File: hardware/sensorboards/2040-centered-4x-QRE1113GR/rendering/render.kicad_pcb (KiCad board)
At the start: 2 copper layers, 204.8 x 52 mm, 44 parts, among them J1 Conn_01x10_Male, U1 QRE1113GR, U2 QRE1113GR, U3 QRE1113GR, U4 QRE1113GR

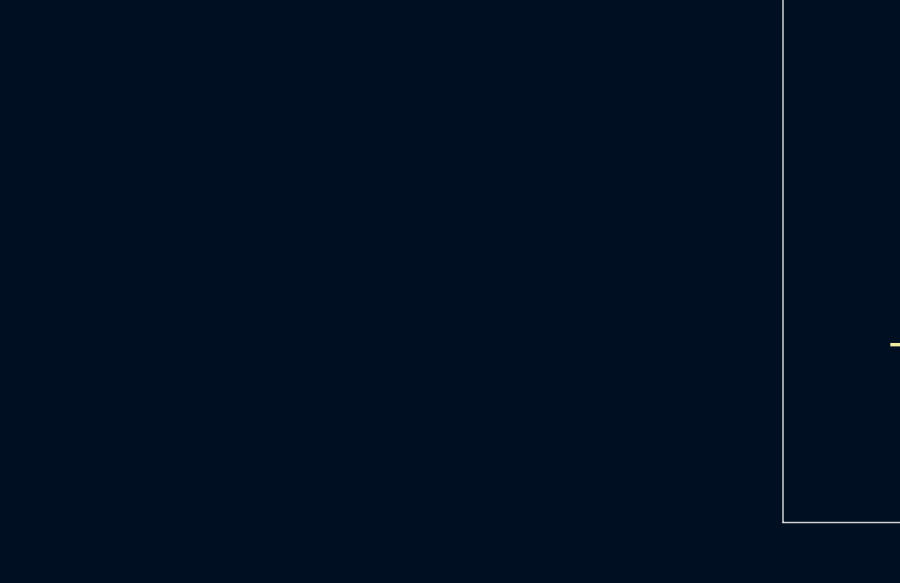
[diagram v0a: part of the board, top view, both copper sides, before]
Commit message: added another screen to show bottom, enlarged mock 3D model of QRE1113 which is not accurate
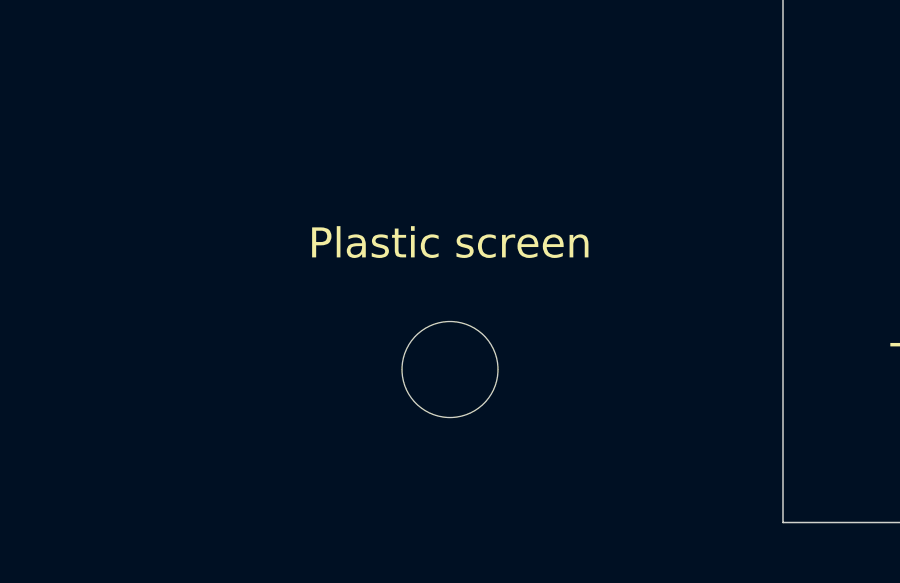
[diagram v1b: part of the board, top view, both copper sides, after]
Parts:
- added Plastic screen: MountingHole, Mounting_Holes:MountingHole_3.2mm_M3, F.Cu at (119.0, 107.2)
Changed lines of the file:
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@@
+    (model "${KICAD6_3DMODEL_DIR}/Package_TO_SOT_SMD.3dshapes/SOT-343_SC-70-4.step"
+      (offset (xyz 0 0 0))
+      (scale (xyz 2.1 1.3 3))
+      (rotate (xyz 0 0 0))
+    )
+  )
+  (footprint "OptoDevice:QRE1113GR" (layer "F.Cu")
+    (at 46.95 92.3)
+    (property "Sheetfile" "2040-centered-4x-QRE1113GR.kicad_sch")
+    (property "Sheetname" "")
+    (attr smd)
+    (fp_text reference "U2" (at 0 2.9 unlocked) (layer "F.SilkS")
+      (effects (font (size 1 1) (thickness 0.15)))
+    )
+    (fp_text value "QRE1113GR" (at 0 4.4 unlocked) (layer "F.Fab")
+      (effects (font (size 1 1) (thickness 0.15)))
+    )
+    (fp_text user "${REFERENCE}" (at 0 0 270 unlocked) (layer "F.Fab")
+      (effects (font (size 0.5 0.5) (thickness 0.075)))
+    )
+    (fp_line (start -1.45 -0.3) (end -1.45 0.3) (layer "F.SilkS") (width 0.24))
+    (fp_line (start -1.45 -1.8) (end 1.45 -1.8) (layer "F.SilkS") (width 0.24))
+    (fp_line (start 1.45 -0.3) (end 1.45 0.3) (layer "F.SilkS") (width 0.24))
+    (fp_line (start 1.45 1.4) (end 1.45 1.8) (layer "F.SilkS") (width 0.24))
+    (fp_line (start 1.45 -1.8) (end 1.45 -1.4) (layer "F.SilkS") (width 0.24))
+    (fp_line (start -0.825 1.8) (end -1.2 1.425) (layer "F.SilkS") (width 0.24))
+    (fp_line (start 1.45 1.8) (end -0.825 1.8) (layer "F.SilkS") (width 0.24))
+    (fp_line (start -1.45 -1.8) (end -1.45 -1.4) (layer "F.SilkS") (width 0.24))
+    (fp_rect (start -3.1 -2.1) (end 3.1 2.1) (layer "F.CrtYd") (width 0.05) (fill none))
+    (fp_line (start 1.45 1.8) (end -0.825 1.8) (layer "F.Fab") (width 0.1))
+    (fp_line (start 1.45 -1.8) (end 1.45 1.8) (layer "F.Fab") (width 0.1))
+    (fp_line (start -0.825 1.8) (end -1.45 1.175) (layer "F.Fab") (width 0.1))
+    (fp_line (start -1.45 1.175) (end -1.45 -1.8) (layer "F.Fab") (width 0.1))
+    (fp_line (start -1.45 -1.8) (end 1.45 -1.8) (layer "F.Fab") (width 0.1))
+    (pad "1" smd roundrect (at -2 0.9) (size 1.66 0.79) (layers "F.Cu" "F.Paste" "F.Mask") (roundrect_rratio 0.05)
+      (net 10 "Net-(TP1-Pad1)") (pinfunction "A") (pintype "passive"))
+    (pad "2" smd roundrect (at 2 0.9) (size 1.66 0.79) (layers "F.Cu" "F.Paste" "F.Mask") (roundrect_rratio 0.05)
+      (net 11 "Net-(TP2-Pad1)") (pinfunction "K") (pintype "passive"))
+    (pad "3" smd roundrect (at 2 -0.9) (size 1.66 0.79) (layers "F.Cu" "F.Paste" "F.Mask") (roundrect_rratio 0.05)
+      (net 13 "Net-(U2-Pad3)") (pintype "open_collector"))
+    (pad "4" smd roundrect (at -2 -0.9) (size 1.66 0.79) (layers "F.Cu" "F.Paste" "F.Mask") (roundrect_rratio 0.05)
+      (net 6 "/E2") (pintype "open_emitter"))
     (model "${KICAD6_3DMODEL_DIR}/Package_TO_SOT_SMD.3dshapes/SOT-343_SC-70-4.step"
       (offset (xyz 0 0 0))
@@
     )
   )
-  (footprint "OptoDevice:QRE1113GR" (layer "F.Cu")
-    (at 46.95 92.3)
-    (property "Sheetfile" "2040-centered-4x-QRE1113GR.kicad_sch")
-    (property "Sheetname" "")
-    (attr smd)
-    (fp_text reference "U2" (at 0 2.9 unlocked) (layer "F.SilkS")
-      (effects (font (size 1 1) (thickness 0.15)))
-    )
-    (fp_text value "QRE1113GR" (at 0 4.4 unlocked) (layer "F.Fab")
-      (effects (font (size 1 1) (thickness 0.15)))
-    )
-    (fp_text user "${REFERENCE}" (at 0 0 270 unlocked) (layer "F.Fab")
-      (effects (font (size 0.5 0.5) (thickness 0.075)))
-    )
-    (fp_line (start -1.45 -0.3) (end -1.45 0.3) (layer "F.SilkS") (width 0.24))
-    (fp_line (start -1.45 -1.8) (end 1.45 -1.8) (layer "F.SilkS") (width 0.24))
-    (fp_line (start 1.45 -0.3) (end 1.45 0.3) (layer "F.SilkS") (width 0.24))
-    (fp_line (start 1.45 1.4) (end 1.45 1.8) (layer "F.SilkS") (width 0.24))
-    (fp_line (start 1.45 -1.8) (end 1.45 -1.4) (layer "F.SilkS") (width 0.24))
-    (fp_line (start -0.825 1.8) (end -1.2 1.425) (layer "F.SilkS") (width 0.24))
-    (fp_line (start 1.45 1.8) (end -0.825 1.8) (layer "F.SilkS") (width 0.24))
-    (fp_line (start -1.45 -1.8) (end -1.45 -1.4) (layer "F.SilkS") (width 0.24))
-    (fp_rect (start -3.1 -2.1) (end 3.1 2.1) (layer "F.CrtYd") (width 0.05) (fill none))
-    (fp_line (start 1.45 1.8) (end -0.825 1.8) (layer "F.Fab") (width 0.1))
-    (fp_line (start 1.45 -1.8) (end 1.45 1.8) (layer "F.Fab") (width 0.1))
-    (fp_line (start -0.825 1.8) (end -1.45 1.175) (layer "F.Fab") (width 0.1))
-    (fp_line (start -1.45 1.175) (end -1.45 -1.8) (layer "F.Fab") (width 0.1))
-    (fp_line (start -1.45 -1.8) (end 1.45 -1.8) (layer "F.Fab") (width 0.1))
-    (pad "1" smd roundrect (at -2 0.9) (size 1.66 0.79) (layers "F.Cu" "F.Paste" "F.Mask") (roundrect_rratio 0.05)
-      (net 10 "Net-(TP1-Pad1)") (pinfunction "A") (pintype "passive"))
-    (pad "2" smd roundrect (at 2 0.9) (size 1.66 0.79) (layers "F.Cu" "F.Paste" "F.Mask") (roundrect_rratio 0.05)
-      (net 11 "Net-(TP2-Pad1)") (pinfunction "K") (pintype "passive"))
-    (pad "3" smd roundrect (at 2 -0.9) (size 1.66 0.79) (layers "F.Cu" "F.Paste" "F.Mask") (roundrect_rratio 0.05)
-      (net 13 "Net-(U2-Pad3)") (pintype "open_collector"))
-    (pad "4" smd roundrect (at -2 -0.9) (size 1.66 0.79) (layers "F.Cu" "F.Paste" "F.Mask") (roundrect_rratio 0.05)
-      (net 6 "/E2") (pintype "open_emitter"))
-    (model "${KICAD6_3DMODEL_DIR}/Package_TO_SOT_SMD.3dshapes/SOT-343_SC-70-4.step"
-      (offset (xyz 0 0 0))
-      (scale (xyz 2.1 1.3 1.5))
-      (rotate (xyz 0 0 0))
+  (footprint "Mounting_Holes:MountingHole_3.2mm_M3" (layer "F.Cu")
+    (at 119 107.2)
+    (descr "Mounting Hole 3.2mm, no annular, M3")
+    (tags "mounting hole 3.2mm no annular m3")
+    (property "Sheetfile" "2040-centered-4x-QRE1113GR.kicad_sch")
+    (property "Sheetname" "")
+    (attr exclude_from_pos_files)
+    (fp_text reference "Plastic screen" (at 0 -4.2) (layer "F.SilkS")
+      (effects (font (size 1 1) (thickness 0.15)))
+    )
+    (fp_text value "MountingHole" (at 0 4.2) (layer "F.Fab")
+      (effects (font (size 1 1) (thickness 0.15)))
+    )
+    (fp_circle (center 0 0) (end 3.2 0) (layer "Cmts.User") (width 0.15) (fill none))
+    (fp_circle (center 0 0) (end 3.45 0) (layer "F.CrtYd") (width 0.05) (fill none))
+    (pad "" np_thru_hole circle (at 0 0) (size 3.2 3.2) (drill 3.2) (layers *.Cu *.Mask))
+    (model "${KIPRJMOD}/QRE1113-screen.wrl"
+      (offset (xyz -59 -12.3 0))
+      (scale (xyz 1 1 1))
+      (rotate (xyz -90 0 -30))
     )
   )
@@
     (model "${KICAD6_3DMODEL_DIR}/Package_TO_SOT_SMD.3dshapes/SOT-343_SC-70-4.step"
       (offset (xyz 0 0 0))
-      (scale (xyz 2.1 1.3 1.5))
+      (scale (xyz 2.1 1.3 3))
       (rotate (xyz 0 0 0))
     )
@@
     (model "${KICAD6_3DMODEL_DIR}/Package_TO_SOT_SMD.3dshapes/SOT-343_SC-70-4.step"
       (offset (xyz 0 0 0))
-      (scale (xyz 2.1 1.3 1.5))
+      (scale (xyz 2.1 1.3 3))
       (rotate (xyz 0 0 0))
     )
@@
     (model "${KICAD6_3DMODEL_DIR}/Package_TO_SOT_SMD.3dshapes/SOT-343_SC-70-4.step"
       (offset (xyz 0 0 0))
-      (scale (xyz 2.1 1.3 1.5))
-      (rotate (xyz 0 0 0))
-    )
+      (scale (xyz 2.1 1.3 3))
+      (rotate (xyz 0 0 0))
+    )

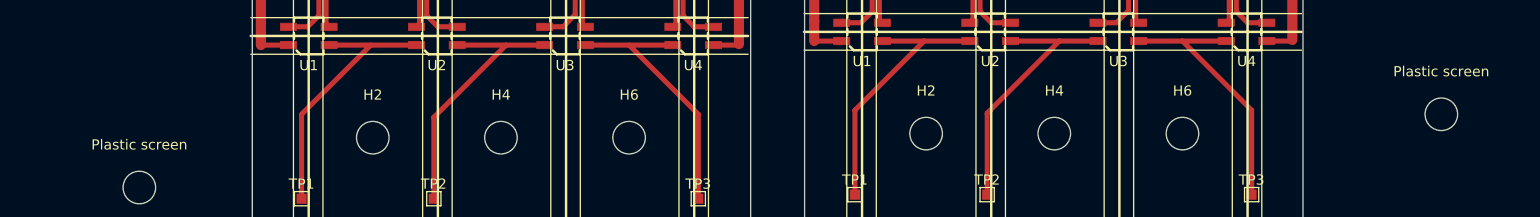
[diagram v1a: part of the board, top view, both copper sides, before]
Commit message: protector is a clearer word than screen
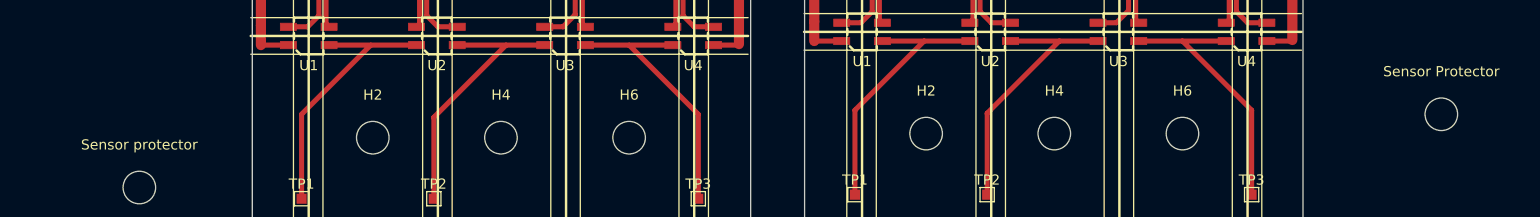
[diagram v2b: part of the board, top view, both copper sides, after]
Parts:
- Sensor Protector: renamed from Plastic screen
- Sensor protector: renamed from Plastic screen
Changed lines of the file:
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@@
     (property "Sheetname" "")
     (attr exclude_from_pos_files)
-    (fp_text reference "Plastic screen" (at 0 -4.2) (layer "F.SilkS")
+    (fp_text reference "Sensor protector" (at 0 -4.2) (layer "F.SilkS")
       (effects (font (size 1 1) (thickness 0.15)))
     )
@@
     (fp_circle (center 0 0) (end 3.45 0) (layer "F.CrtYd") (width 0.05) (fill none))
     (pad "" np_thru_hole circle (at 0 0) (size 3.2 3.2) (drill 3.2) (layers *.Cu *.Mask))
-    (model "${KIPRJMOD}/QRE1113-screen.wrl"
+    (model "${KIPRJMOD}/QRE1113-protector.wrl"
       (offset (xyz -59 -12.3 0))
       (scale (xyz 1 1 1))
@@
     (property "Sheetname" "")
     (attr exclude_from_pos_files)
-    (fp_text reference "Plastic screen" (at 0 -4.2) (layer "F.SilkS")
+    (fp_text reference "Sensor Protector" (at 0 -4.2) (layer "F.SilkS")
       (effects (font (size 1 1) (thickness 0.15)))
     )
@@
     (fp_circle (center 0 0) (end 3.45 0) (layer "F.CrtYd") (width 0.05) (fill none))
     (pad "" np_thru_hole circle (at 0 0) (size 3.2 3.2) (drill 3.2) (layers *.Cu *.Mask))
-    (model "${KIPRJMOD}/QRE1113-screen.wrl"
+    (model "${KIPRJMOD}/QRE1113-protector.wrl"
       (offset (xyz -116.9 -12.3 0))
       (scale (xyz 1 1 1))
